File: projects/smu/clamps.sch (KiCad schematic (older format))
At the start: 35 parts, among them P401 CONN_01X34, U401 DAC8734, U402 LM324, U404 LM324, U405 DG444

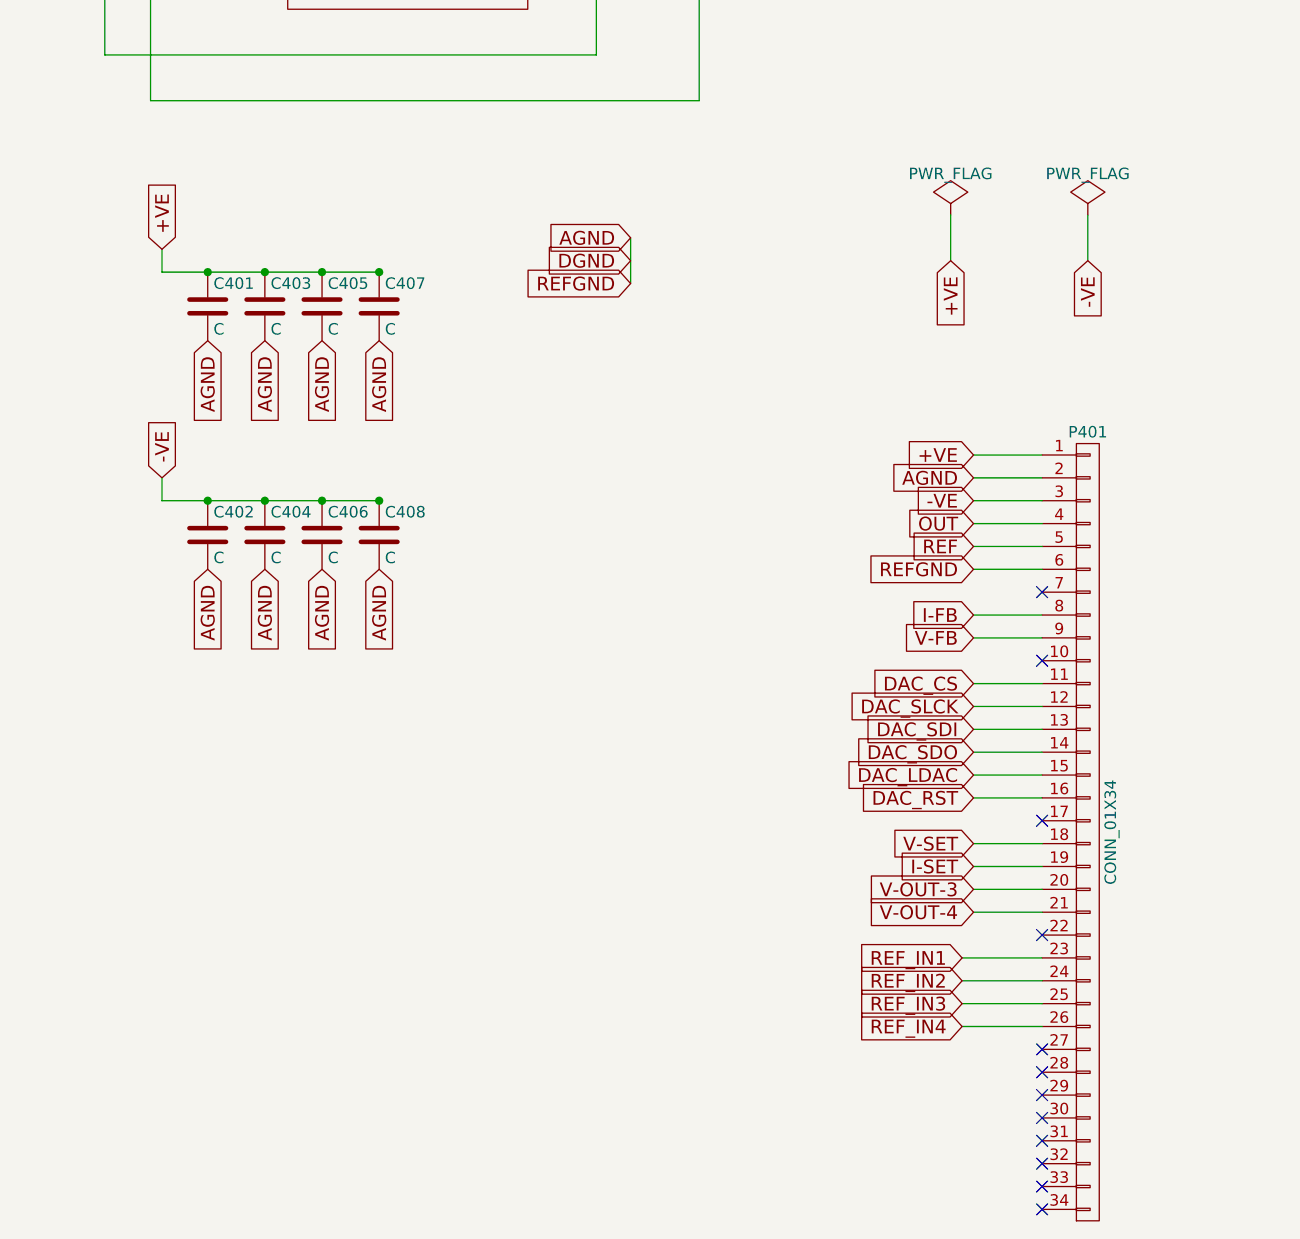
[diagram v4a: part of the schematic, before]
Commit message: pulled out the connectors to the top sheet
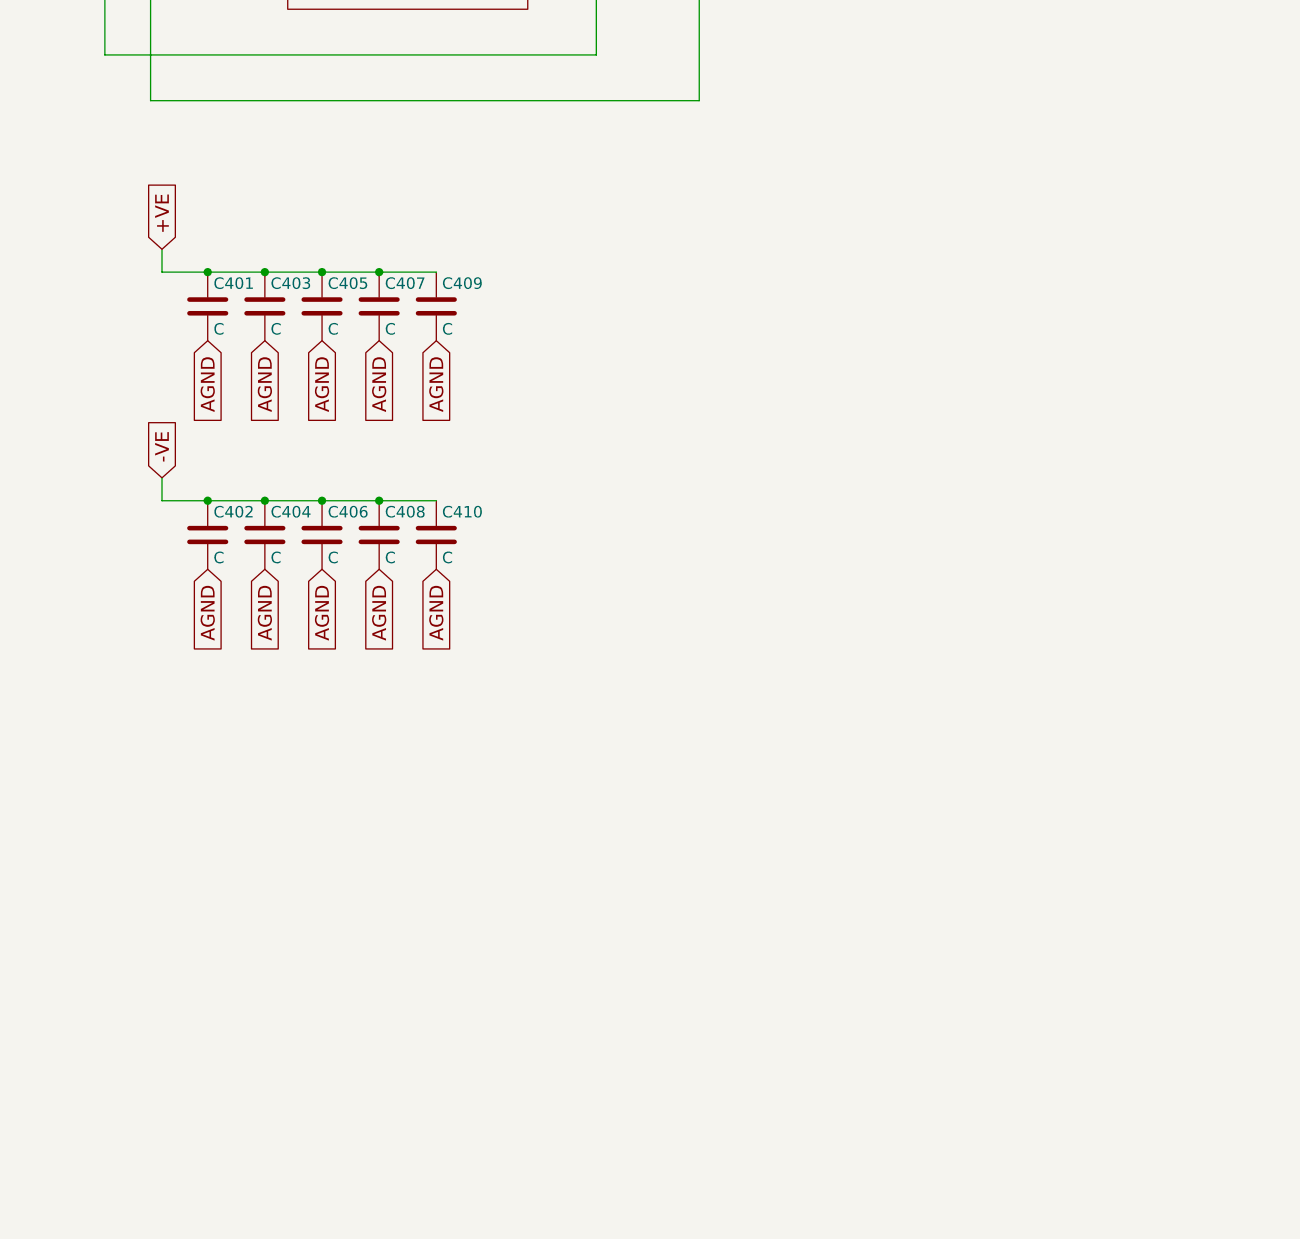
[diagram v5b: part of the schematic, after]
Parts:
- removed P401: CONN_01X34, symbol CONN_01X34
- added C409, C410: C, Capacitors_SMD:C_1206, symbol C
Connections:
- net +VE: now also C409.1
- net -VE: now also C410.1
- net AGND: now also C409.2, C410.2; no longer R403.1, U401.11 (DGND), U401.18 (SGND-0), U401.20 (SGND-1), U401.29 (REFGND-A), U401.32 (REFGND-B), U401.41 (SGND-3), U401.43 (SGND-2)
- new net DGND: U401.11 (DGND)
- new net REFGND: R403.1, U401.18 (SGND-0), U401.20 (SGND-1), U401.29 (REFGND-A), U401.32 (REFGND-B), U401.41 (SGND-3), U401.43 (SGND-2)
- no-connect marks 35 -> 23
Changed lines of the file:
@@
 Text GLabel 1800 5050 1    60   Input ~ 0
-+VE
-Text GLabel 5350 5950 0    60   Input ~ 0
 +VE
 NoConn ~ 11550 2100
@@
 	12350 3100 12950 3100
 Connection ~ 12700 2450
-Text GLabel 5350 6150 0    60   Input ~ 0
--VE
 Text GLabel 7900 1500 0    60   Input ~ 0
 I-FB
@@
 	1800 5050 1800 5150
 Wire Wire Line
-	1800 5150 2750 5150
+	1800 5150 3000 5150
 Connection ~ 2000 5150
 Text GLabel 2000 5450 3    60   Input ~ 0
@@
 	1800 6050 1800 6150
 Wire Wire Line
-	1800 6150 2750 6150
+	1800 6150 3000 6150
 Connection ~ 2000 6150
 Text GLabel 2000 6450 3    60   Input ~ 0
@@
 Text GLabel 1800 6050 1    60   Input ~ 0
 -VE
-Text GLabel 5350 6050 0    60   Input ~ 0
-AGND
-Text GLabel 5350 6350 0    60   Input ~ 0
-REF
-Wire Wire Line
-	5650 5950 5350 5950
-Wire Wire Line
-	5650 6050 5350 6050
-Wire Wire Line
-	5650 6150 5350 6150
-Wire Wire Line
-	5650 6250 5350 6250
-Text GLabel 5350 6650 0    60   Input ~ 0
-I-FB
 Connection ~ 12700 3100
 Text GLabel 12950 3100 2    60   Input ~ 0
 OUT
-Text GLabel 5350 6250 0    60   Input ~ 0
-OUT
-NoConn ~ 5650 6850
 NoConn ~ 11550 4700
 NoConn ~ 11650 4700
@@
 Text GLabel 7900 4300 0    60   Input ~ 0
 V-FB
-Text GLabel 5350 6750 0    60   Input ~ 0
-V-FB
 Wire Wire Line
 	12700 5700 12300 5700
 Connection ~ 2750 5150
 Connection ~ 2750 6150
-Wire Wire Line
-	5350 6350 5650 6350
-Wire Wire Line
-	5650 6750 5350 6750
 Wire Wire Line
 	10600 1500 10400 1500
@@
 Text GLabel 4300 3500 2    60   Input ~ 0
 V-OUT-4
-Wire Wire Line
-	5350 6650 5650 6650
 $Comp
 L LM324 U402
@@
 Text GLabel 9150 2700 1    60   Input ~ 0
 +VE
-Text GLabel 5250 5100 3    60   Input ~ 0
-+VE
-$Comp
-L PWR_FLAG #FLG01
-U 1 1 58AA88D7
-P 5250 4900
-F 0 "#FLG01" H 5250 4995 50  0001 C CNN
-F 1 "PWR_FLAG" H 5250 5080 50  0000 C CNN
-F 2 "" H 5250 4900 50  0000 C CNN
-F 3 "" H 5250 4900 50  0000 C CNN
-	1    5250 4900
-	1    0    0    -1
-$EndComp
-Wire Wire Line
-	5250 4900 5250 5100
-$Comp
-L PWR_FLAG #FLG02
-U 1 1 58AAC503
-P 5850 4900
-F 0 "#FLG02" H 5850 4995 50  0001 C CNN
-F 1 "PWR_FLAG" H 5850 5080 50  0000 C CNN
-F 2 "" H 5850 4900 50  0000 C CNN
-F 3 "" H 5850 4900 50  0000 C CNN
-	1    5850 4900
-	1    0    0    -1
-$EndComp
-Text GLabel 5850 5100 3    60   Input ~ 0
--VE
-Wire Wire Line
-	5850 4900 5850 5100
-Text GLabel 5350 7850 0    60   Input ~ 0
-V-OUT-3
-Text GLabel 5350 7950 0    60   Input ~ 0
-V-OUT-4
-Text GLabel 5350 6950 0    60   Input ~ 0
-DAC_CS
-Text GLabel 5350 7050 0    60   Input ~ 0
-DAC_SLCK
-Text GLabel 5350 7150 0    60   Input ~ 0
-DAC_SDI
-Text GLabel 5350 7250 0    60   Input ~ 0
-DAC_SDO
-Text GLabel 5350 7350 0    60   Input ~ 0
-DAC_LDAC
-Text GLabel 5350 7450 0    60   Input ~ 0
-DAC_RST
-Wire Wire Line
-	5350 6950 5650 6950
-Wire Wire Line
-	5350 7050 5650 7050
-Wire Wire Line
-	5350 7150 5650 7150
-Wire Wire Line
-	5350 7250 5650 7250
-Wire Wire Line
-	5350 7350 5650 7350
-Wire Wire Line
-	5350 7450 5650 7450
 Text GLabel 1400 1700 0    60   Input ~ 0
 DAC_CS
@@
 Wire Wire Line
 	1400 2200 2100 2200
-Text GLabel 3850 5000 0    60   Input ~ 0
-AGND
-Text GLabel 3850 5100 0    60   Input ~ 0
-DGND
-Text GLabel 3850 5200 0    60   Input ~ 0
-REFGND
-Wire Wire Line
-	3850 5000 3850 5200
-Wire Wire Line
-	5350 7650 5650 7650
-Wire Wire Line
-	5350 7750 5650 7750
-Text GLabel 5350 7650 0    60   Input ~ 0
-V-SET
-Text GLabel 5350 7750 0    60   Input ~ 0
-I-SET
-Wire Wire Line
-	5350 7850 5650 7850
-Wire Wire Line
-	5350 7950 5650 7950
-NoConn ~ 5650 6550
-NoConn ~ 5650 7550
 Text GLabel 7350 2900 2    60   Input ~ 0
 +VE
@@
 	7000 3100 7350 3100
 $Comp
-L CONN_01X34 P401
-U 1 1 58AECC4E
-P 5850 7600
-F 0 "P401" H 5850 9350 50  0000 C CNN
-F 1 "CONN_01X34" V 5950 7600 50  0000 C CNN
-F 2 "" H 5850 7600 50  0000 C CNN
-F 3 "" H 5850 7600 50  0000 C CNN
-	1    5850 7600
-	1    0    0    -1
-$EndComp
-Text GLabel 5300 8150 0    60   Input ~ 0
-REF_IN1
-Text GLabel 5300 8250 0    60   Input ~ 0
-REF_IN2
-Text GLabel 5300 8350 0    60   Input ~ 0
-REF_IN3
-Text GLabel 5300 8450 0    60   Input ~ 0
-REF_IN4
-Wire Wire Line
-	5300 8150 5650 8150
-Wire Wire Line
-	5300 8250 5650 8250
-Wire Wire Line
-	5300 8350 5650 8350
-Wire Wire Line
-	5300 8450 5650 8450
-NoConn ~ 5650 8050
-NoConn ~ 5650 8550
-NoConn ~ 5650 8650
-NoConn ~ 5650 8750
-NoConn ~ 5650 8850
-NoConn ~ 5650 8950
-NoConn ~ 5650 9050
-NoConn ~ 5650 9150
-NoConn ~ 5650 9250
-$Comp
 L C C407
 U 1 1 58AEEE25
@@
 Text GLabel 2750 6450 3    60   Input ~ 0
 AGND
-Text GLabel 5350 6450 0    60   Input ~ 0
-REFGND
-Wire Wire Line
-	5350 6450 5650 6450
 Wire Wire Line
 	5800 2800 5550 2800
@@
 	1    0    0    -1
 $EndComp
+$Comp
+L C C409
+U 1 1 58A9EA17
+P 3000 5300
+F 0 "C409" H 3025 5400 50  0000 L CNN
+F 1 "C" H 3025 5200 50  0000 L CNN
+F 2 "Capacitors_SMD:C_1206" H 3038 5150 50  0001 C CNN
+F 3 "" H 3000 5300 50  0000 C CNN
+	1    3000 5300
+	1    0    0    -1
+$EndComp
+Text GLabel 3000 5450 3    60   Input ~ 0
+AGND
+$Comp
+L C C410
+U 1 1 58A9ED73
+P 3000 6300
+F 0 "C410" H 3025 6400 50  0000 L CNN
+F 1 "C" H 3025 6200 50  0000 L CNN
+F 2 "Capacitors_SMD:C_1206" H 3038 6150 50  0001 C CNN
+F 3 "" H 3000 6300 50  0000 C CNN
+	1    3000 6300
+	1    0    0    -1
+$EndComp
+Text GLabel 3000 6450 3    60   Input ~ 0
+AGND
 $EndSCHEMATC

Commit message: generate net and parts
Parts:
- U402, U404: footprint (none) -> Housings_SOIC:SOIC-14_3.9x8.7mm_Pitch1.27mm
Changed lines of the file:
@@
 F 0 "U402" H 9250 3200 50  0000 L CNN
 F 1 "LM324" H 9250 2800 50  0000 L CNN
-F 2 "" H 9200 3100 50  0000 C CNN
+F 2 "Housings_SOIC:SOIC-14_3.9x8.7mm_Pitch1.27mm" H 9200 3100 50  0001 C CNN
 F 3 "" H 9300 3200 50  0000 C CNN
 	3    9250 3000
@@
 F 0 "U402" H 9250 5800 50  0000 L CNN
 F 1 "LM324" H 9250 5400 50  0000 L CNN
-F 2 "" H 9200 5700 50  0000 C CNN
+F 2 "Housings_SOIC:SOIC-14_3.9x8.7mm_Pitch1.27mm" H 9200 5700 50  0001 C CNN
 F 3 "" H 9300 5800 50  0000 C CNN
 	4    9250 5600
@@
 F 0 "U402" H 9850 7450 50  0000 L CNN
 F 1 "LM324" H 9850 7050 50  0000 L CNN
-F 2 "" H 9800 7350 50  0000 C CNN
+F 2 "Housings_SOIC:SOIC-14_3.9x8.7mm_Pitch1.27mm" H 9800 7350 50  0001 C CNN
 F 3 "" H 9900 7450 50  0000 C CNN
 	2    9850 7250
@@
 F 0 "U402" H 8900 7450 50  0000 L CNN
 F 1 "LM324" H 8900 7050 50  0000 L CNN
-F 2 "" H 8850 7350 50  0000 C CNN
+F 2 "Housings_SOIC:SOIC-14_3.9x8.7mm_Pitch1.27mm" H 8850 7350 50  0001 C CNN
 F 3 "" H 8950 7450 50  0000 C CNN
 	1    8900 7250
@@
 F 0 "U404" H 11550 5900 50  0000 L CNN
 F 1 "LM324" H 11550 5500 50  0000 L CNN
-F 2 "" H 11500 5800 50  0000 C CNN
+F 2 "Housings_SOIC:SOIC-14_3.9x8.7mm_Pitch1.27mm" H 11500 5800 50  0001 C CNN
 F 3 "" H 11600 5900 50  0000 C CNN
 	4    11550 5700
@@
 F 0 "U404" H 11550 4600 50  0000 L CNN
 F 1 "LM324" H 11550 4200 50  0000 L CNN
-F 2 "" H 11500 4500 50  0000 C CNN
+F 2 "Housings_SOIC:SOIC-14_3.9x8.7mm_Pitch1.27mm" H 11500 4500 50  0001 C CNN
 F 3 "" H 11600 4600 50  0000 C CNN
 	3    11550 4400
@@
 F 0 "U404" H 11550 3300 50  0000 L CNN
 F 1 "LM324" H 11550 2900 50  0000 L CNN
-F 2 "" H 11500 3200 50  0000 C CNN
+F 2 "Housings_SOIC:SOIC-14_3.9x8.7mm_Pitch1.27mm" H 11500 3200 50  0001 C CNN
 F 3 "" H 11600 3300 50  0000 C CNN
 	2    11550 3100
@@
 F 0 "U404" H 11550 2000 50  0000 L CNN
 F 1 "LM324" H 11550 1600 50  0000 L CNN
-F 2 "" H 11500 1900 50  0000 C CNN
+F 2 "Housings_SOIC:SOIC-14_3.9x8.7mm_Pitch1.27mm" H 11500 1900 50  0001 C CNN
 F 3 "" H 11600 2000 50  0000 C CNN
 	1    11550 1800

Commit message: add nettie library etc
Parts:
- W401, W402: footprint conn-test:NET-TIE -> NET-TIE
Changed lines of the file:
@@
 F 0 "W402" H 7350 3050 50  0000 C CNN
 F 1 "NET-TIE" H 7350 2950 50  0000 C CNN
-F 2 "conn-test:NET-TIE" H 7350 2700 50  0001 C CNN
+F 2 "NET-TIE" H 7350 2700 50  0001 C CNN
 F 3 "" H 7350 2800 60  0000 C CNN
 	1    7350 2800
@@
 F 0 "W401" H 5450 3050 50  0000 C CNN
 F 1 "NET-TIE" H 5450 2950 50  0000 C CNN
-F 2 "conn-test:NET-TIE" H 5450 2700 50  0001 C CNN
+F 2 "NET-TIE" H 5450 2700 50  0001 C CNN
 F 3 "" H 5450 2800 60  0000 C CNN
 	1    5450 2800

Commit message: change resistors to all 1206
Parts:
- W401, W402: footprint NET-TIE -> footprint:NET-TIE-0.3mm
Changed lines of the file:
@@
 F 0 "W402" H 7350 3050 50  0000 C CNN
 F 1 "NET-TIE" H 7350 2950 50  0000 C CNN
-F 2 "NET-TIE" H 7350 2700 50  0001 C CNN
+F 2 "footprint:NET-TIE-0.3mm" H 7350 2700 50  0001 C CNN
 F 3 "" H 7350 2800 60  0000 C CNN
 	1    7350 2800
@@
 F 0 "W401" H 5450 3050 50  0000 C CNN
 F 1 "NET-TIE" H 5450 2950 50  0000 C CNN
-F 2 "NET-TIE" H 5450 2700 50  0001 C CNN
+F 2 "footprint:NET-TIE-0.3mm" H 5450 2700 50  0001 C CNN
 F 3 "" H 5450 2800 60  0000 C CNN
 	1    5450 2800
